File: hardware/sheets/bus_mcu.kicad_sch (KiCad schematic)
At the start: 22 parts, among them U1 RP2350B, U10 74HCT163, U11 74HCT163, U12 74HCT165, U2 74LVC245A, U3 74LVC245A, U4 74LVC245A, U5 74LVC245A, U6 74LVC245A, U7 74HCT163, U8 74HCT163, U9 74HCT163

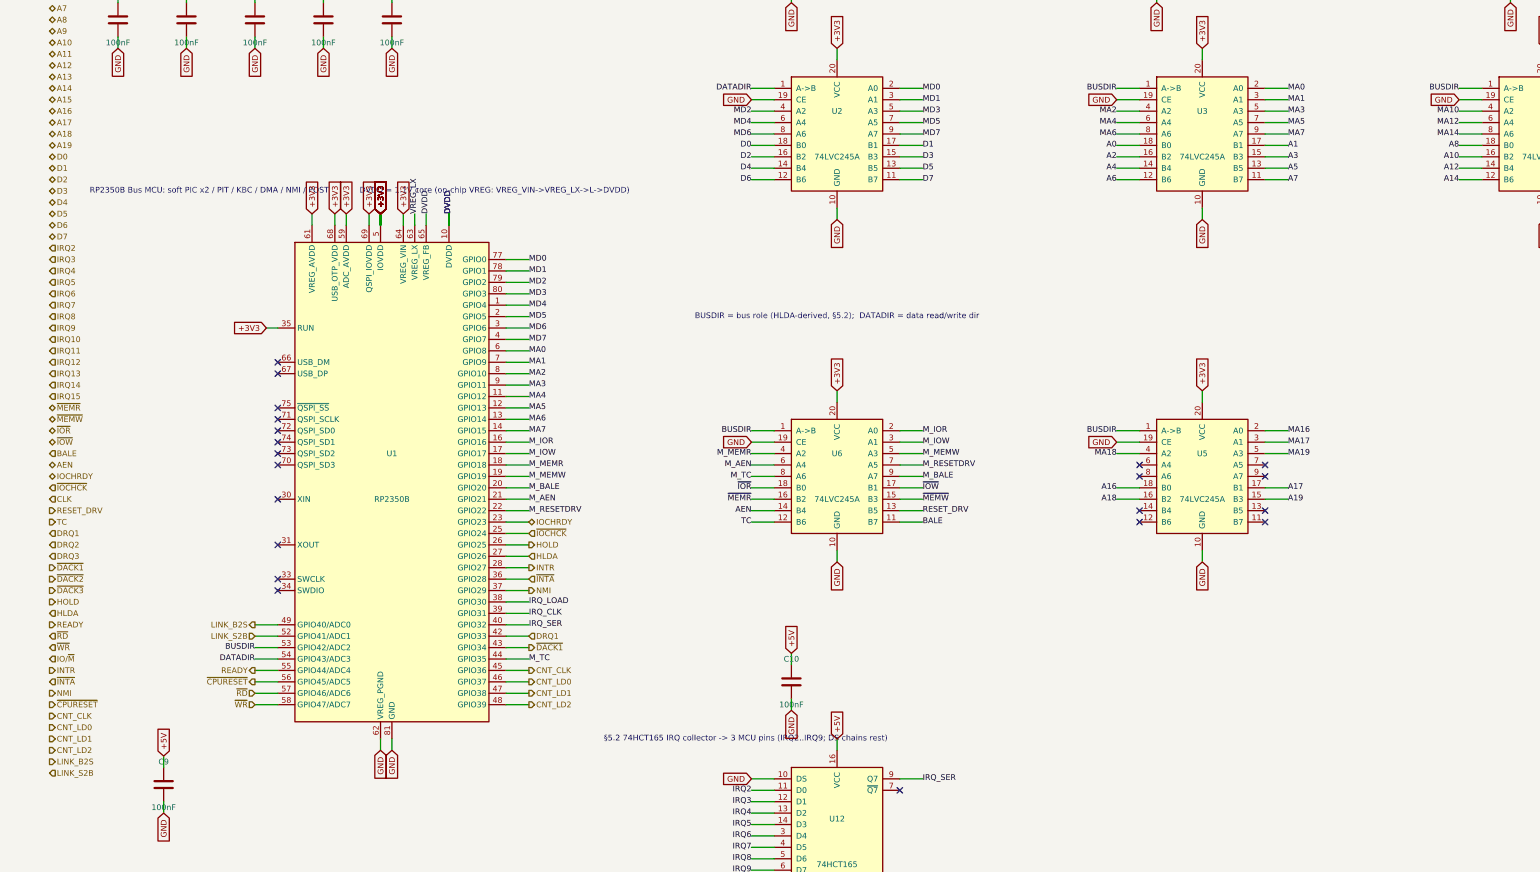
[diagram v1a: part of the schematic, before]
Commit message: Move speed-select latch from Supervisor to Bus MCU
SPEED_SEL now originates on the Bus MCU (GPIO42) and drives the cpu_core clock
mux; the Supervisor sends the divisor choice over the UART link instead, dropping
its cross-sheet interface to the 2-wire link + power. To stay within the 48-GPIO
budget, the address/control transceiver direction is now HLDA-derived externally
(per S5.2) rather than a dedicated BUSDIR GPIO. Bus MCU now owns both reset
sequencing and speed-select. Netlist verified; zero structural ERC errors.

Co-Authored-By: Claude Opus 4.8 (1M context) <noreply@anthropic.com>
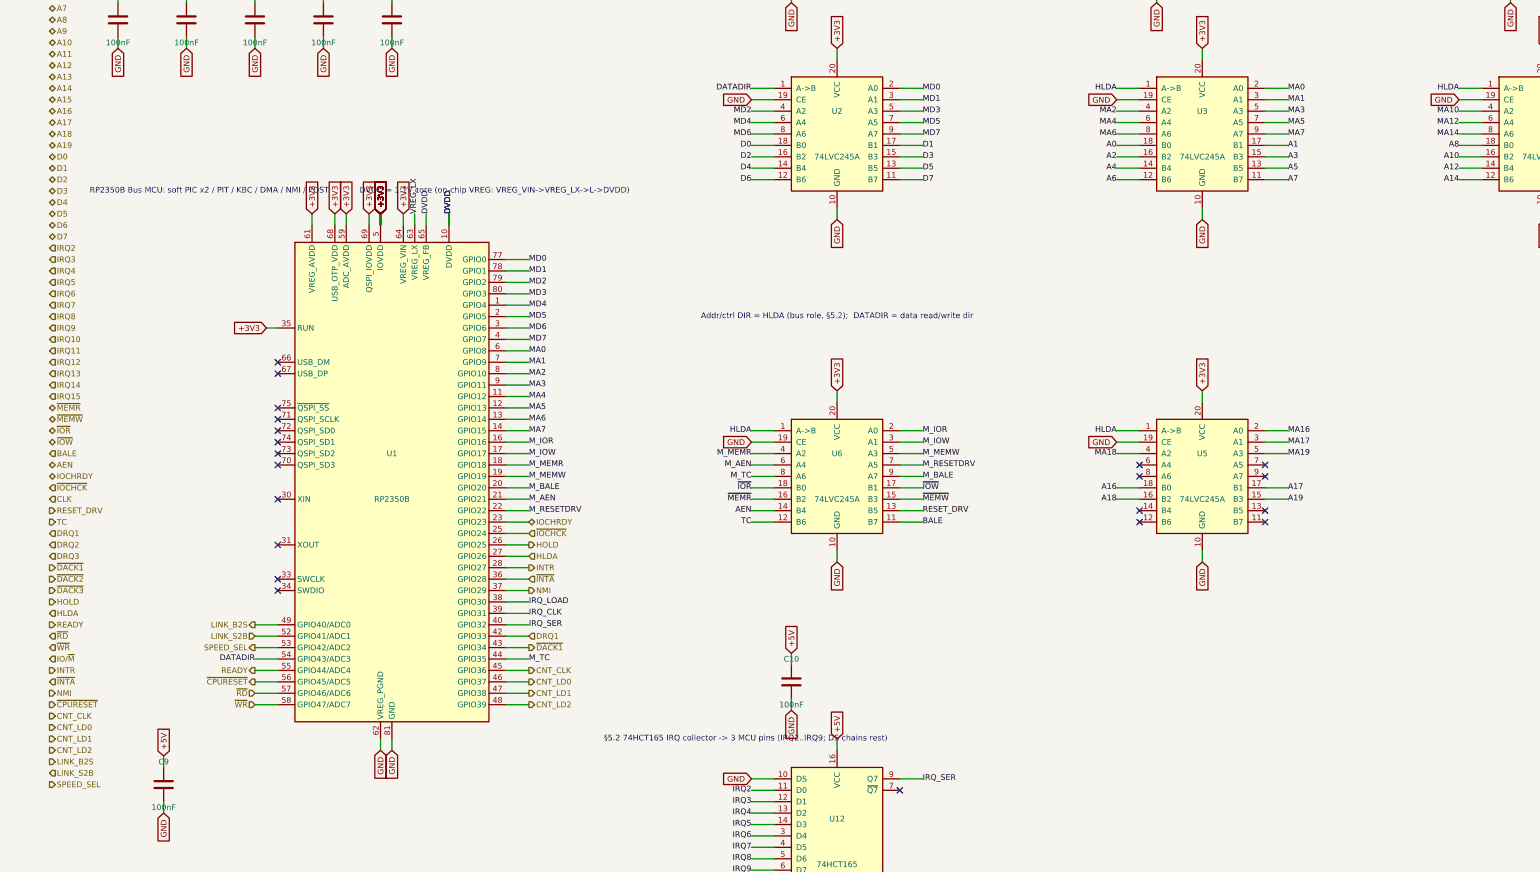
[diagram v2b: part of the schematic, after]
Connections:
- net HLDA: now also U3.1 (A->B), U4.1 (A->B), U5.1 (A->B), U6.1 (A->B)
- removed net BUSDIR: U1.53 (GPIO42/ADC2), U3.1 (A->B), U4.1 (A->B), U5.1 (A->B), U6.1 (A->B)
- new net SPEED_SEL: U1.53 (GPIO42/ADC2)
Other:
- note added: "Addr/ctrl DIR = HLDA (bus role, §5.2); DATADIR = data read/write dir"
- note removed: "BUSDIR = bus role (HLDA-derived, §5.2); DATADIR = data read/write dir"
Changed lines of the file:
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@@
 		)
 	)
+	(hierarchical_label "SPEED_SEL"
+		(shape output)
+		(at 25.4 220.98 0)
+		(effects
+			(font
+				(size 1.27 1.27)
+			)
+		)
+	)
 	(wire
 		(pts
@@
 		)
 	)
-	(label "BUSDIR"
+	(hierarchical_label "SPEED_SEL"
+		(shape output)
 		(at 71.12 190.5 180)
 		(effects
@@
 		)
 	)
-	(label "BUSDIR"
+	(label "HLDA"
 		(at 181.61 142.24 180)
 		(effects
@@
 		)
 	)
-	(label "BUSDIR"
+	(label "HLDA"
 		(at 262.89 66.04 180)
 		(effects
@@
 		)
 	)
-	(label "BUSDIR"
+	(label "HLDA"
 		(at 339.09 66.04 180)
 		(effects
@@
 		)
 	)
-	(label "BUSDIR"
+	(label "HLDA"
 		(at 262.89 142.24 180)
 		(effects
@@
 		)
 	)
-	(text "BUSDIR = bus role (HLDA-derived, §5.2);  DATADIR = data read/write dir"
+	(text "Addr/ctrl DIR = HLDA (bus role, §5.2);  DATADIR = data read/write dir"
 		(at 200.66 116.84 0)
 		(effects
@@
 		(instances
 			(project "mini-xt"
-				(path "/12a90590-121b-4b08-bc73-62c223de1072/e50d0a17-50fb-4006-9356-a8363e32698a"
+				(path "/e080ba29-8ec9-4601-9572-fbaf5ae0d583/566aa91e-bb61-4a33-aec1-8b4c0f139e0e"
 					(reference "U201")
 					(unit 1)
@@
 		(instances
 			(project "mini-xt"
-				(path "/12a90590-121b-4b08-bc73-62c223de1072/e50d0a17-50fb-4006-9356-a8363e32698a"
+				(path "/e080ba29-8ec9-4601-9572-fbaf5ae0d583/566aa91e-bb61-4a33-aec1-8b4c0f139e0e"
 					(reference "U202")
 					(unit 1)
@@
 		(instances
 			(project "mini-xt"
-				(path "/12a90590-121b-4b08-bc73-62c223de1072/e50d0a17-50fb-4006-9356-a8363e32698a"
+				(path "/e080ba29-8ec9-4601-9572-fbaf5ae0d583/566aa91e-bb61-4a33-aec1-8b4c0f139e0e"
 					(reference "U206")
 					(unit 1)
@@
 		(instances
 			(project "mini-xt"
-				(path "/12a90590-121b-4b08-bc73-62c223de1072/e50d0a17-50fb-4006-9356-a8363e32698a"
+				(path "/e080ba29-8ec9-4601-9572-fbaf5ae0d583/566aa91e-bb61-4a33-aec1-8b4c0f139e0e"
 					(reference "U203")
 					(unit 1)
@@
 		(instances
 			(project "mini-xt"
-				(path "/12a90590-121b-4b08-bc73-62c223de1072/e50d0a17-50fb-4006-9356-a8363e32698a"
+				(path "/e080ba29-8ec9-4601-9572-fbaf5ae0d583/566aa91e-bb61-4a33-aec1-8b4c0f139e0e"
 					(reference "U204")
 					(unit 1)
@@
 		(instances
 			(project "mini-xt"
-				(path "/12a90590-121b-4b08-bc73-62c223de1072/e50d0a17-50fb-4006-9356-a8363e32698a"
+				(path "/e080ba29-8ec9-4601-9572-fbaf5ae0d583/566aa91e-bb61-4a33-aec1-8b4c0f139e0e"
 					(reference "U205")
 					(unit 1)
@@
 		(instances
 			(project "mini-xt"
-				(path "/12a90590-121b-4b08-bc73-62c223de1072/e50d0a17-50fb-4006-9356-a8363e32698a"
+				(path "/e080ba29-8ec9-4601-9572-fbaf5ae0d583/566aa91e-bb61-4a33-aec1-8b4c0f139e0e"
 					(reference "U207")
 					(unit 1)
@@
 		(instances
 			(project "mini-xt"
-				(path "/12a90590-121b-4b08-bc73-62c223de1072/e50d0a17-50fb-4006-9356-a8363e32698a"
+				(path "/e080ba29-8ec9-4601-9572-fbaf5ae0d583/566aa91e-bb61-4a33-aec1-8b4c0f139e0e"
 					(reference "U208")
 					(unit 1)
@@
 		(instances
 			(project "mini-xt"
-				(path "/12a90590-121b-4b08-bc73-62c223de1072/e50d0a17-50fb-4006-9356-a8363e32698a"
+				(path "/e080ba29-8ec9-4601-9572-fbaf5ae0d583/566aa91e-bb61-4a33-aec1-8b4c0f139e0e"
 					(reference "U209")
 					(unit 1)
@@
 		(instances
 			(project "mini-xt"
-				(path "/12a90590-121b-4b08-bc73-62c223de1072/e50d0a17-50fb-4006-9356-a8363e32698a"
+				(path "/e080ba29-8ec9-4601-9572-fbaf5ae0d583/566aa91e-bb61-4a33-aec1-8b4c0f139e0e"
 					(reference "U210")
 					(unit 1)
@@
 		(instances
 			(project "mini-xt"
-				(path "/12a90590-121b-4b08-bc73-62c223de1072/e50d0a17-50fb-4006-9356-a8363e32698a"
+				(path "/e080ba29-8ec9-4601-9572-fbaf5ae0d583/566aa91e-bb61-4a33-aec1-8b4c0f139e0e"
 					(reference "U211")
 					(unit 1)
@@
 		(instances
 			(project "mini-xt"
-				(path "/12a90590-121b-4b08-bc73-62c223de1072/e50d0a17-50fb-4006-9356-a8363e32698a"
+				(path "/e080ba29-8ec9-4601-9572-fbaf5ae0d583/566aa91e-bb61-4a33-aec1-8b4c0f139e0e"
 					(reference "U212")
 					(unit 1)
@@
 		(instances
 			(project "mini-xt"
-				(path "/12a90590-121b-4b08-bc73-62c223de1072/e50d0a17-50fb-4006-9356-a8363e32698a"
+				(path "/e080ba29-8ec9-4601-9572-fbaf5ae0d583/566aa91e-bb61-4a33-aec1-8b4c0f139e0e"
 					(reference "C201")
 					(unit 1)
@@
 		(instances
 			(project "mini-xt"
-				(path "/12a90590-121b-4b08-bc73-62c223de1072/e50d0a17-50fb-4006-9356-a8363e32698a"
+				(path "/e080ba29-8ec9-4601-9572-fbaf5ae0d583/566aa91e-bb61-4a33-aec1-8b4c0f139e0e"
 					(reference "C202")
 					(unit 1)
@@
 		(instances
 			(project "mini-xt"
-				(path "/12a90590-121b-4b08-bc73-62c223de1072/e50d0a17-50fb-4006-9356-a8363e32698a"
+				(path "/e080ba29-8ec9-4601-9572-fbaf5ae0d583/566aa91e-bb61-4a33-aec1-8b4c0f139e0e"
 					(reference "C203")
 					(unit 1)
@@
 		(instances
 			(project "mini-xt"
-				(path "/12a90590-121b-4b08-bc73-62c223de1072/e50d0a17-50fb-4006-9356-a8363e32698a"
+				(path "/e080ba29-8ec9-4601-9572-fbaf5ae0d583/566aa91e-bb61-4a33-aec1-8b4c0f139e0e"
 					(reference "C204")
 					(unit 1)
@@
 		(instances
 			(project "mini-xt"
-				(path "/12a90590-121b-4b08-bc73-62c223de1072/e50d0a17-50fb-4006-9356-a8363e32698a"
+				(path "/e080ba29-8ec9-4601-9572-fbaf5ae0d583/566aa91e-bb61-4a33-aec1-8b4c0f139e0e"
 					(reference "C205")
 					(unit 1)
@@
 		(instances
 			(project "mini-xt"
-				(path "/12a90590-121b-4b08-bc73-62c223de1072/e50d0a17-50fb-4006-9356-a8363e32698a"
+				(path "/e080ba29-8ec9-4601-9572-fbaf5ae0d583/566aa91e-bb61-4a33-aec1-8b4c0f139e0e"
 					(reference "C206")
 					(unit 1)
@@
 		(instances
 			(project "mini-xt"
-				(path "/12a90590-121b-4b08-bc73-62c223de1072/e50d0a17-50fb-4006-9356-a8363e32698a"
+				(path "/e080ba29-8ec9-4601-9572-fbaf5ae0d583/566aa91e-bb61-4a33-aec1-8b4c0f139e0e"
 					(reference "C207")
 					(unit 1)
@@
 		(instances
 			(project "mini-xt"
-				(path "/12a90590-121b-4b08-bc73-62c223de1072/e50d0a17-50fb-4006-9356-a8363e32698a"
+				(path "/e080ba29-8ec9-4601-9572-fbaf5ae0d583/566aa91e-bb61-4a33-aec1-8b4c0f139e0e"
 					(reference "C208")
 					(unit 1)
@@
 		(instances
 			(project "mini-xt"
-				(path "/12a90590-121b-4b08-bc73-62c223de1072/e50d0a17-50fb-4006-9356-a8363e32698a"
+				(path "/e080ba29-8ec9-4601-9572-fbaf5ae0d583/566aa91e-bb61-4a33-aec1-8b4c0f139e0e"
 					(reference "C209")
 					(unit 1)
@@
 		(instances
 			(project "mini-xt"
-				(path "/12a90590-121b-4b08-bc73-62c223de1072/e50d0a17-50fb-4006-9356-a8363e32698a"
+				(path "/e080ba29-8ec9-4601-9572-fbaf5ae0d583/566aa91e-bb61-4a33-aec1-8b4c0f139e0e"
 					(reference "C210")
 					(unit 1)

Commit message: Use Waveshare Core2350B modules for both RP2350B nodes
Replace the bare RP2350B on bus_mcu and video with the Core2350B module
(mini-xt:Core2350B, 64-pin PGA, all 48 GPIO + power/control). Each module takes
+5V on VBUS and self-generates 3V3 (onboard ME6217 LDO) that powers its own local
level shifters (3V3_BUS/3V3_VID, sheet-local, not paralleled). Bus MCU uses the
0MB-PSRAM variant (GPIO47 free); video uses the 8MB variant (onboard PSRAM is the
VGA aperture, discrete APS6404 removed). Drops the per-site core SMPS/inductor,
flash, and crystal. Netlist verified; modules self-power from +5V; zero structural
ERC errors.

Co-Authored-By: Claude Opus 4.8 (1M context) <noreply@anthropic.com>
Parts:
- removed C4, C5: 100nF, symbol Device:C
- removed U1: RP2350B, symbol MCU_RaspberryPi:RP2350B
- added M1: Core2350B (0MB PSRAM), symbol mini-xt:Core2350B
- C3: value 100nF -> 10uF
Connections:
- net +3V3: no longer C1.1, C2.1, C3.1, C6.1, C7.1, U2.20 (VCC), U3.20 (VCC), U4.20 (VCC), U5.20 (VCC), U6.20 (VCC)
- net +5V: now also M1.49 (VBUS)
- net CNT_CLK: now also M1.37 (GPIO36)
- net CNT_LD0: now also M1.38 (GPIO37)
- net CNT_LD1: now also M1.39 (GPIO38)
- net CNT_LD2: now also M1.40 (GPIO39)
- net DATADIR: now also M1.44 (GPIO43)
- net DRQ1: now also M1.34 (GPIO33)
- net GND: now also M1.59 (GND), M1.60 (GND)
- net HLDA: now also M1.27 (GPIO26)
- net HOLD: now also M1.26 (GPIO25)
- net INTR: now also M1.28 (GPIO27)
- net IOCHRDY: now also M1.24 (GPIO23)
- net IRQ_CLK: now also M1.32 (GPIO31)
- net IRQ_LOAD: now also M1.31 (GPIO30)
- net IRQ_SER: now also M1.33 (GPIO32)
- net LINK_B2S: now also M1.41 (GPIO40)
- net LINK_S2B: now also M1.42 (GPIO41)
- net MA0: now also M1.9 (GPIO8)
- net MA1: now also M1.10 (GPIO9)
- net MA2: now also M1.11 (GPIO10)
- net MA3: now also M1.12 (GPIO11)
- net MA4: now also M1.13 (GPIO12)
- net MA5: now also M1.14 (GPIO13)
- net MA6: now also M1.15 (GPIO14)
- net MA7: now also M1.16 (GPIO15)
- net MD0: now also M1.1 (GPIO0)
- net MD1: now also M1.2 (GPIO1)
- net MD2: now also M1.3 (GPIO2)
- net MD3: now also M1.4 (GPIO3)
- net MD4: now also M1.5 (GPIO4)
- net MD5: now also M1.6 (GPIO5)
- net MD6: now also M1.7 (GPIO6)
- net MD7: now also M1.8 (GPIO7)
- net M_AEN: now also M1.22 (GPIO21)
- net M_BALE: now also M1.21 (GPIO20)
- net M_IOR: now also M1.17 (GPIO16)
- net M_IOW: now also M1.18 (GPIO17)
- net M_MEMR: now also M1.19 (GPIO18)
- net M_MEMW: now also M1.20 (GPIO19)
- net M_RESETDRV: now also M1.23 (GPIO22)
- net M_TC: now also M1.36 (GPIO35)
- net NMI: now also M1.30 (GPIO29)
- net READY: now also M1.45 (GPIO44)
- net SPEED_SEL: now also M1.43 (GPIO42)
- net ~{CPURESET}: now also M1.46 (GPIO45)
- net ~{DACK1}: now also M1.35 (GPIO34)
- net ~{INTA}: now also M1.29 (GPIO28)
- net ~{IOCHCK}: now also M1.25 (GPIO24)
- net ~{RD}: now also M1.47 (GPIO46)
- net ~{WR}: now also M1.48 (GPIO47)
- new net 3V3_BUS: C1.1, C2.1, C3.1, C6.1, C7.1, M1.50 (3V3), U2.20 (VCC), U3.20 (VCC), U4.20 (VCC), U5.20 (VCC), U6.20 (VCC)
- no-connect marks 22 -> 18
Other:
- note added: "Core2350B module (RP2350B): soft PIC x2 / PIT / KBC / DMA / NMI / POST."
- note added: "Self-powers 3V3 from +5V (onboard ME6217 LDO); user LED on GPIO39 (=CNT_LD2)."
- note removed: "DVDD = 1.1V core (on-chip VREG: VREG_VIN->VREG_LX->L->DVDD)"
- note removed: "RP2350B Bus MCU: soft PIC x2 / PIT / KBC / DMA / NMI / POST"
